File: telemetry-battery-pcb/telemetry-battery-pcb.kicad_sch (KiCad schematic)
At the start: 67 parts, among them J1 Network Connector, J3 CONN_360410_MZC, J5 CONN_360410_MZC, Q1 NMOS, Q2 PMOS, Q4 NMOS, U4 LTC2944, U5 XR76208, U6 M24C02-WMN, U7 TPS1HTC30-Q1

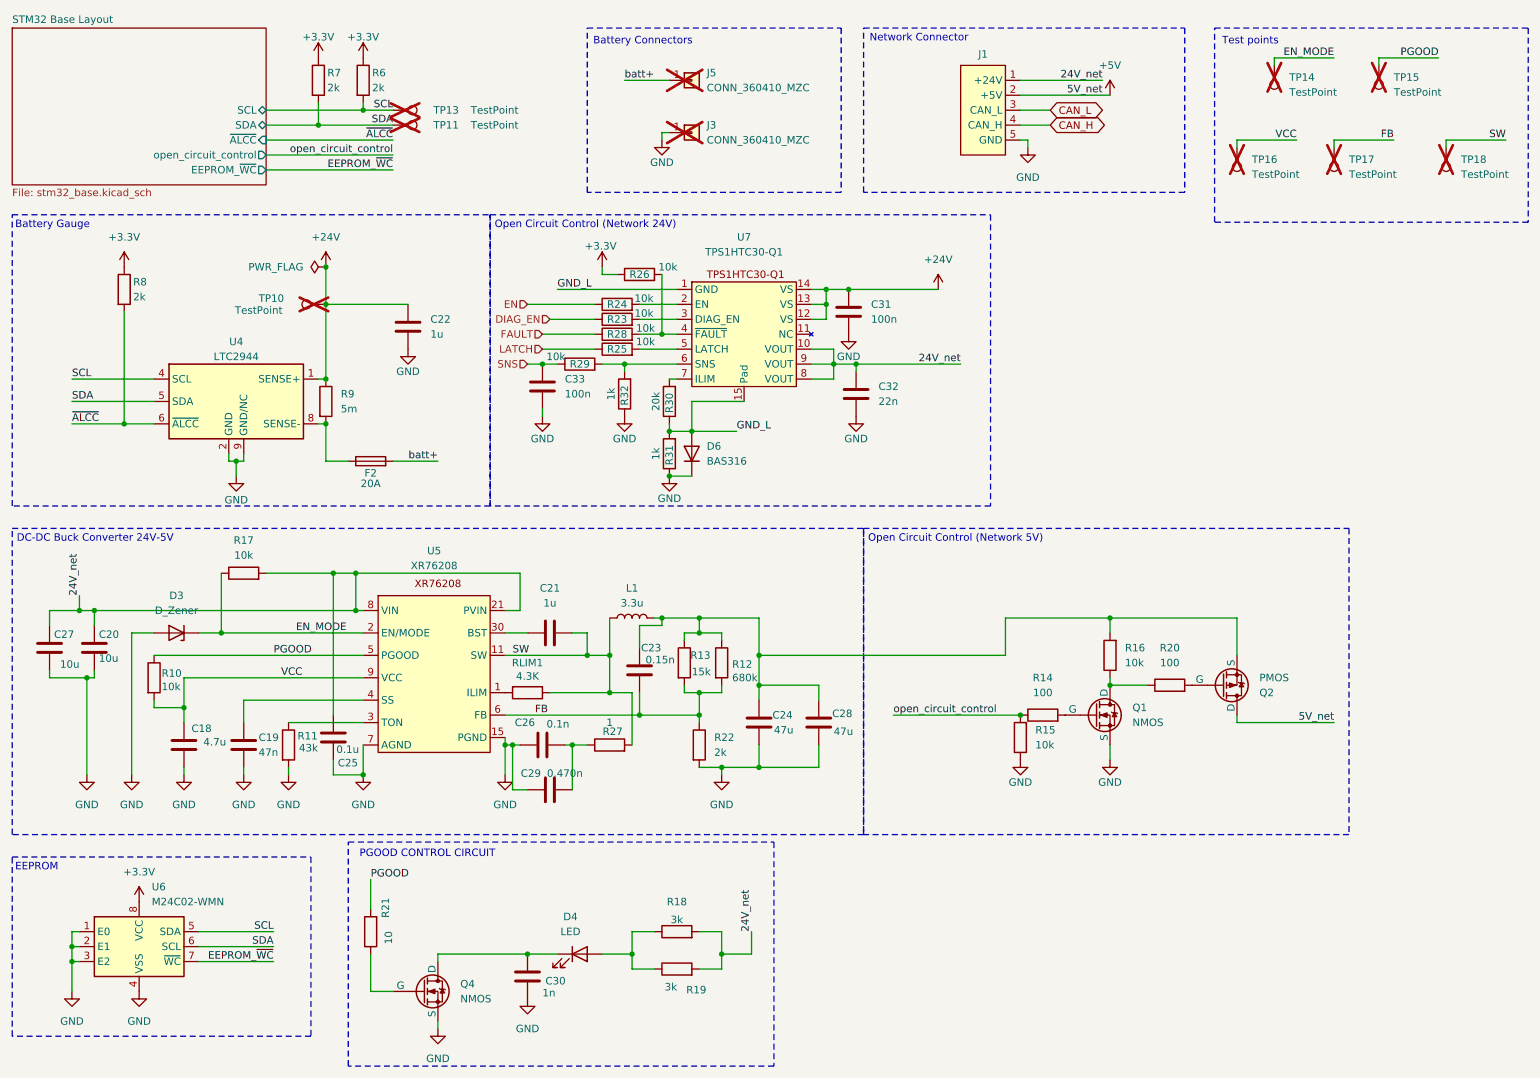
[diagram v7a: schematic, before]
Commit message: telemetry-battery-pcb: review schematic and pcb
Changes:
- Reduce the value of fuse F2 to 10A (no impact on footprint or JLCPCB
  number)
- Group all test points together (and relevant changes to PCB)
  - +24V test point
  - I2C test points (SDA and SCL)
- Change the 24V-network used as input for the 5V DC-DC (and relevant
  changes to PCB). The STM32 on this PCB needs to be powered on (using
  the 5V-network) in ordrer to enable the 24V-net output for other PCBs.
  Therefore, the DC-DC converter needs to be supplied directly from the
  battery, as described in the TPS1HTC30 datasheet.
- Change the position of the +5V power label (and relevant changes to
  PCB). The reasoning is similar to the previous point. The 5V_NET is
  controlled by the STM32 itself, which therefore needs to be powered on
  separately.
- Change the 24V-network used for the PGOOD LED (results from changing
  the 24V-nework input to the DC-DC converter). PCB was also updated to
  reflect these changes.
- Connect the TPS1HTC30 I/O to STM32. There was an incompatibility with
  the labels used which meant KiCad didn't properly connect the nets.
  Now we have local labels in the root page, connected to hierarchical
  labels from the STM32-page. Also swapped the pin used by SNS to PA0,
  since it needs to be connected to an ADC (PA0 is input 1 of ADC 1).
  PCB was NOT updated accordingly.
- Reorganize and cleaned some labels and text in the schematic
  (alignment, etc.) for clarity.
- Change the style of the DC-DC converter's pin 1 dot in the footprint.
  Also added traces between the inernally connected pins to remove the
  DRC warnings.
- Update PCB metadata (name, code, authors, reviewers, etc.). Also
  updated the text in the Silkscreen for the name of the pcb to match
  what there is in the template.
- Simplify routing in the PCB and removed redundant traces
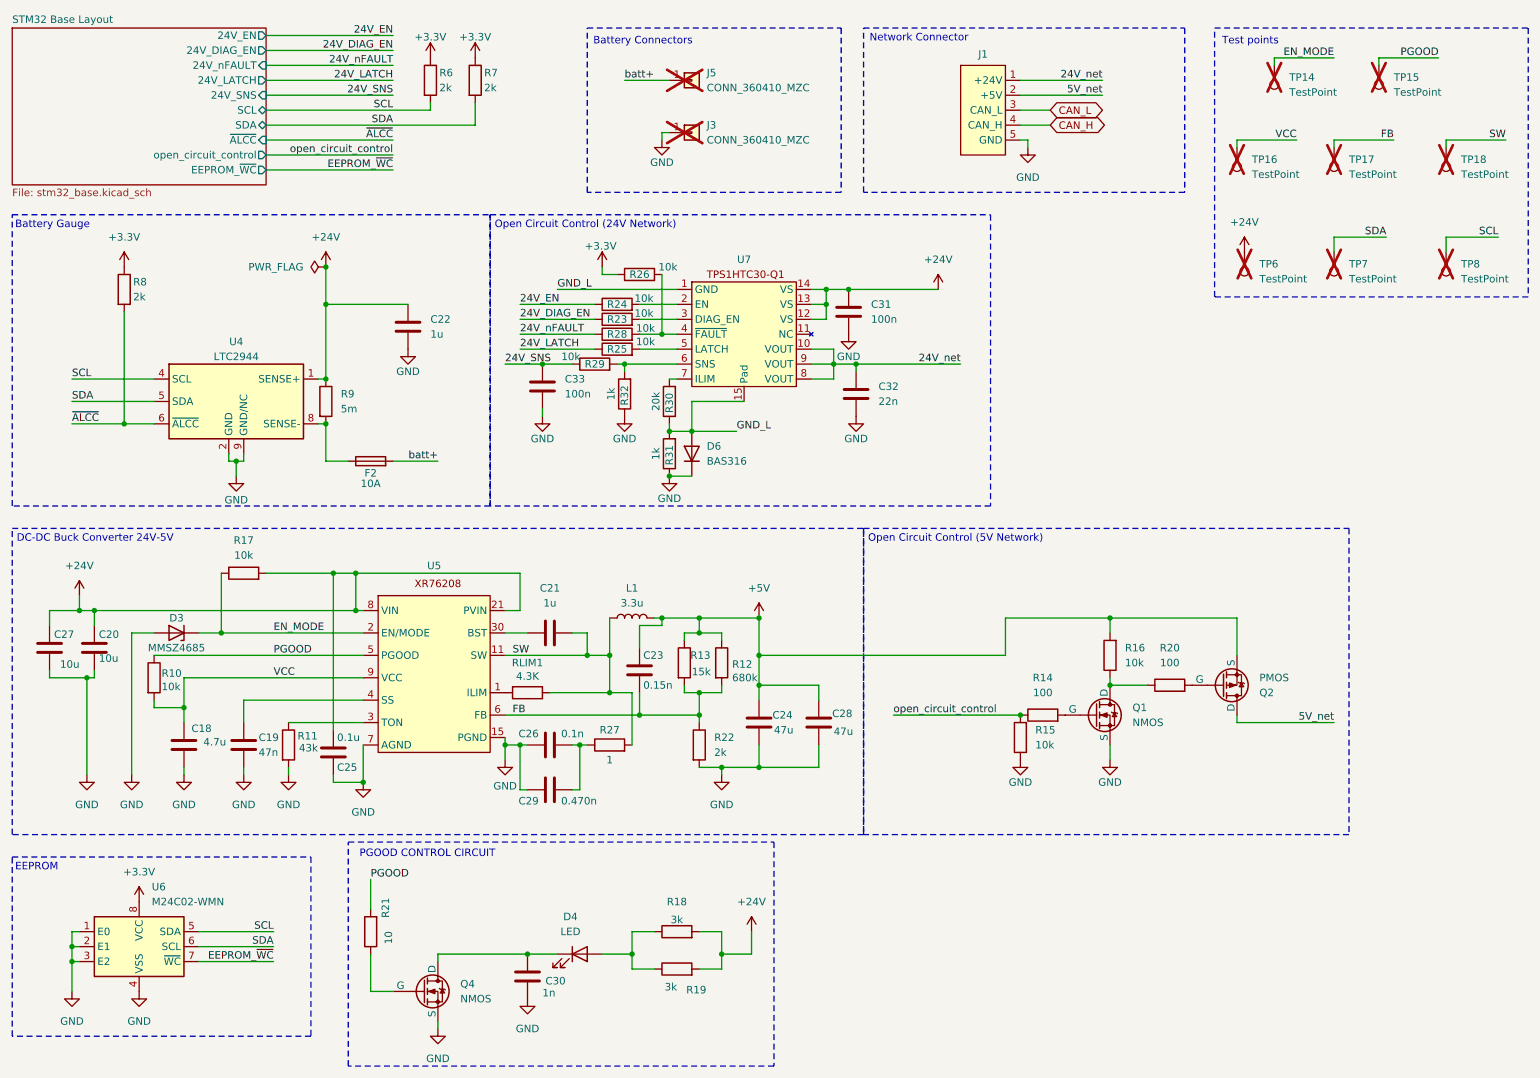
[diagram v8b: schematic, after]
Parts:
- removed TP10, TP11, TP13: TestPoint, TestPoint:TestPoint_Keystone_5005-5009_Compact, symbol Connector:TestPoint
- added TP6, TP7, TP8: TestPoint, TestPoint:TestPoint_Keystone_5005-5009_Compact, symbol Connector:TestPoint
- D3: value D_Zener -> MMSZ4685
- F2: value 20A -> 10A
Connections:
- net +24V: now also C20.1, C25.1, C27.1, R17.2, R18.2, R19.2, U5.21 (PVIN), U5.8 (VIN), TP6.1
- net +5V: now also C23.1, C24.1, C28.1, L1.2, Q2.3 (S), R12.1, R13.1, R16.2; no longer J1.2 (+5V), Q2.1 (D)
- net 24V_net: no longer C20.1, C25.1, C27.1, R17.2, R18.2, R19.2, U5.21 (PVIN), U5.8 (VIN)
- net SCL: now also TP8.1
- net SDA: now also TP7.1
- net DIAG_EN renamed 24V_DIAG_EN
- net EN renamed 24V_EN
- net FAULT renamed 24V_nFAULT
- net LATCH renamed 24V_LATCH
- net SNS renamed 24V_SNS
- new net 5V_net: J1.2 (+5V), Q2.1 (D)
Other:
- sheet STM32 Base Layout ports: added 24V_DIAG_EN, 24V_EN, 24V_LATCH, 24V_SNS, 24V_nFAULT; removed none
- note added: "Open Circuit Control (24V Network)"
- note added: "Open Circuit Control (5V Network)"
- note removed: "Open Circuit Control (Network 24V)"
- note removed: "Open Circuit Control (Network 5V)"
- moved on the sheet: C25, C26, R29, R6, R7
